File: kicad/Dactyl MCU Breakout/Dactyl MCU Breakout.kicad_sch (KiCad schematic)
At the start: 0 parts

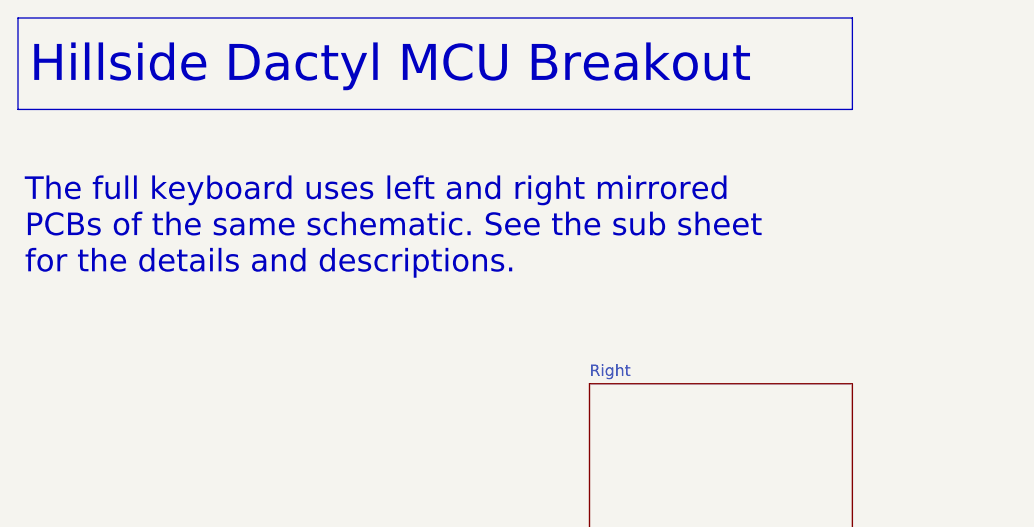
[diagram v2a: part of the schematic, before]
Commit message: feat: area reserved for TRRS. base plate notch
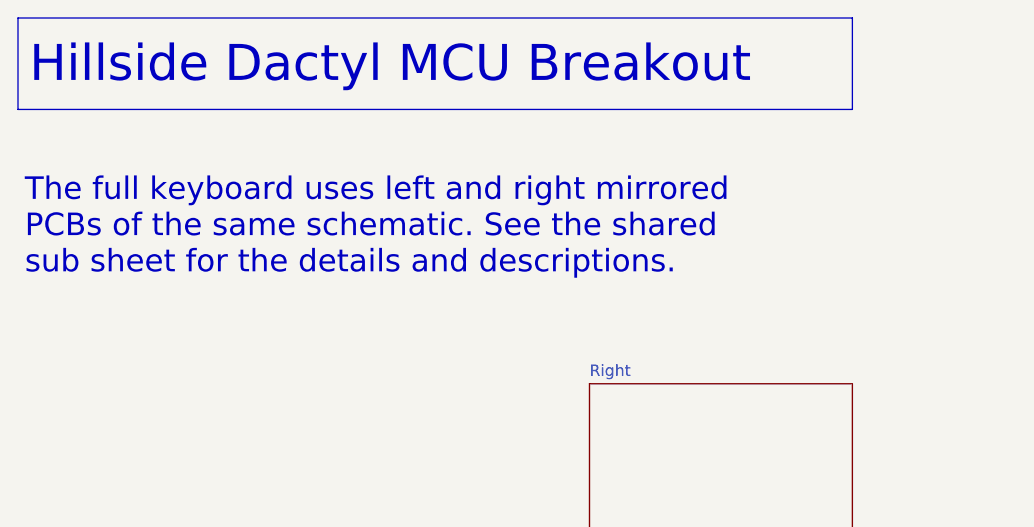
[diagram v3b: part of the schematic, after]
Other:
- note added: "The full keyboard uses left and right mirrored PCBs of the same schematic. See the shared sub sheet for the details and descriptions."
- note removed: "The full keyboard uses left and right mirrored PCBs of the same schematic. See the sub sheet for the details and descriptions."
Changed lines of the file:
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@@
 		)
 	)
-	(text "The full keyboard uses left and right mirrored  \nPCBs of the same schematic. See the sub sheet \nfor the details and descriptions."
+	(text "The full keyboard uses left and right mirrored  \nPCBs of the same schematic. See the shared \nsub sheet for the details and descriptions."
 		(exclude_from_sim no)
 		(at 94.742 99.822 0)

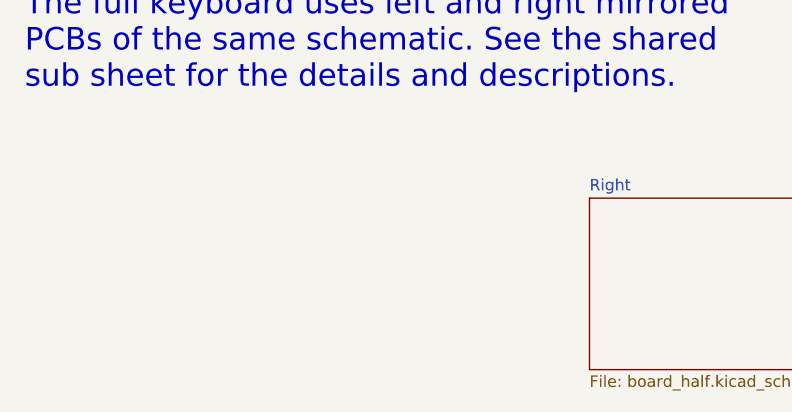
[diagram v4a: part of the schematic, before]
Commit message: feat(pcb): left half re-numbered and some routed
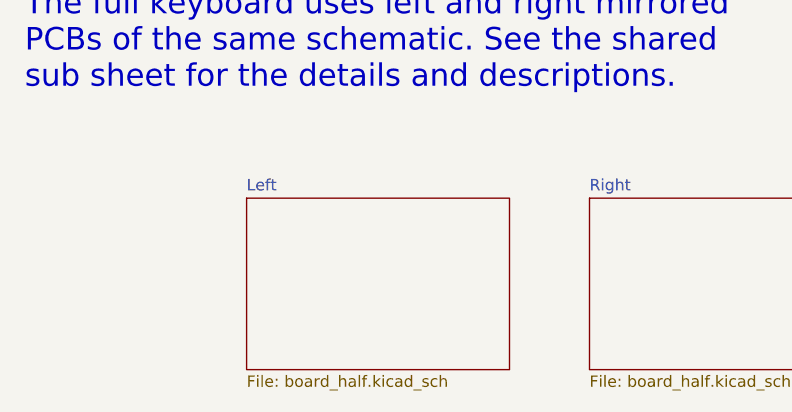
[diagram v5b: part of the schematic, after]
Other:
- added sheet Left (board_half.kicad_sch)
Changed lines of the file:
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@@
+	)
+	(sheet
+		(at 119.38 111.76)
+		(size 29.21 19.05)
+		(fields_autoplaced yes)
+		(stroke
+			(width 0.1524)
+			(type solid)
+		)
+		(fill
+			(color 255 229 191 1.0000)
+		)
+		(property "Sheetname" "Left"
+			(at 119.38 111.0484 0)
+			(effects
+				(font
+					(size 1.27 1.27)
+				)
+				(justify left bottom)
+			)
+		)
+		(property "Sheetfile" "board_half.kicad_sch"
+			(at 119.38 131.3946 0)
+			(effects
+				(font
+					(size 1.27 1.27)
+				)
+				(justify left top)
+			)
+		)
+		(instances
+			(project "Dactyl MCU Breakout"
+				(path "/454146f1-d25e-490f-a0db-4f993607d919"
+					(page "3")
+				)
+			)
+		)
 	)
 	(sheet

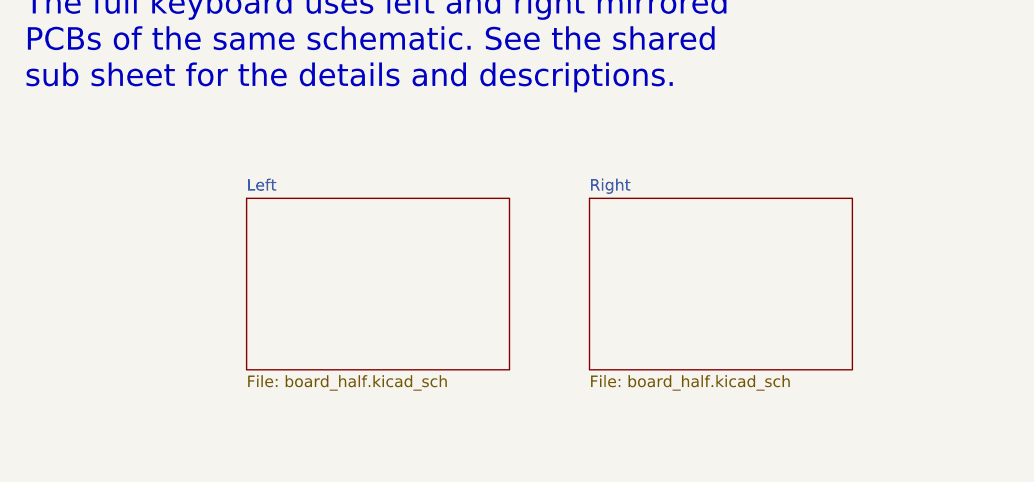
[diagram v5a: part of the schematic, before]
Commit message: feat: handedness jumper only on left board
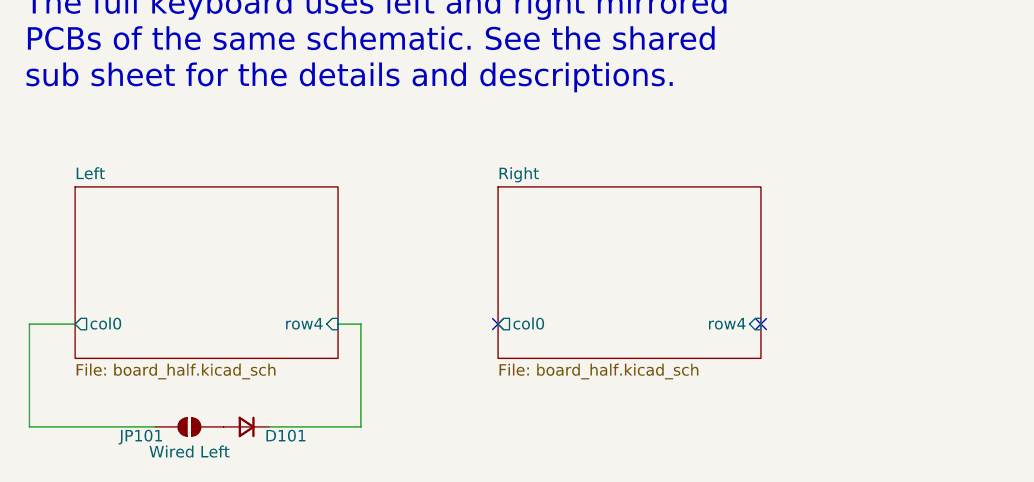
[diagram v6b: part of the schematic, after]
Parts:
- added D101: D_Small, Diode_SMD:D_SOD-323, symbol Device:D_Small
- added JP101: Wired Left, Dactyl_basics:SolderJumper-2_P1.3mm_Open_RoundedPad1.0x1.5mm, symbol Jumper:SolderJumper_2_Open
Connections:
- new net: D101.2 (A), JP101.2 (B)
- new net Left/col0: JP101.1 (A)
- new net Left/row4: D101.1 (K)
- no-connect marks 0 -> 2
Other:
- sheet Left ports: added col0, row4; removed none
- sheet Right ports: added col0, row4; removed none

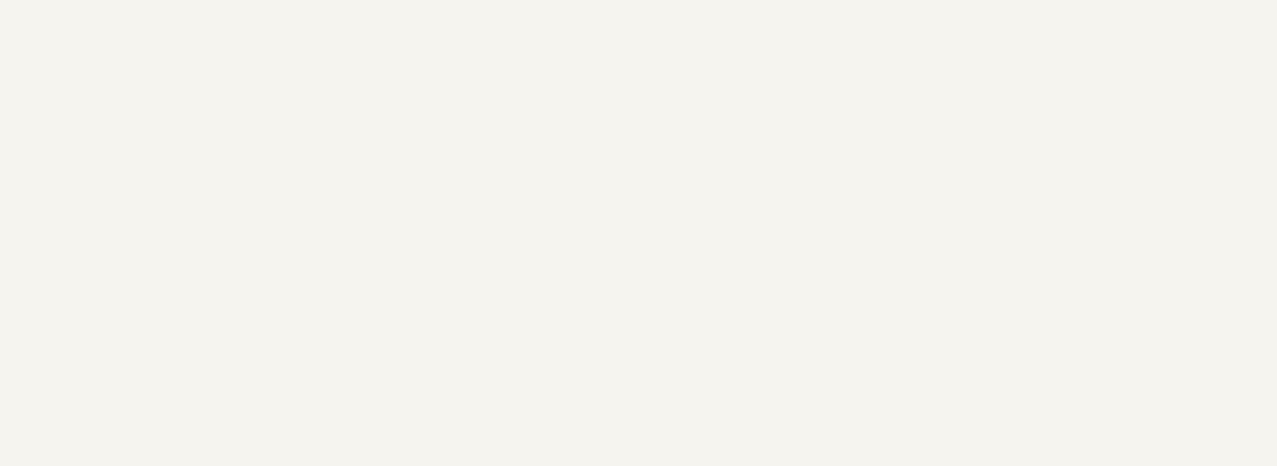
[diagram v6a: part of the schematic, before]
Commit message: feat: larger close capacitors, top/bottom fill
- Solder jumpers for split or battery to reduce the risk of attaching both.
- Wider 0.5 mm tracks for power.
- LED isolation capacitors have smaller loop distance and higher uF within size.
- USB shield ground routed to mount hole pad, as no better place to go.
- Ground fill for top and bottom layers, as well as the middle layer ones.
- Artwork in copper of a small house on a wooded hillside next to a stream.
- Rail copper fills without isolated fill warnings.
- Test point for split data line.
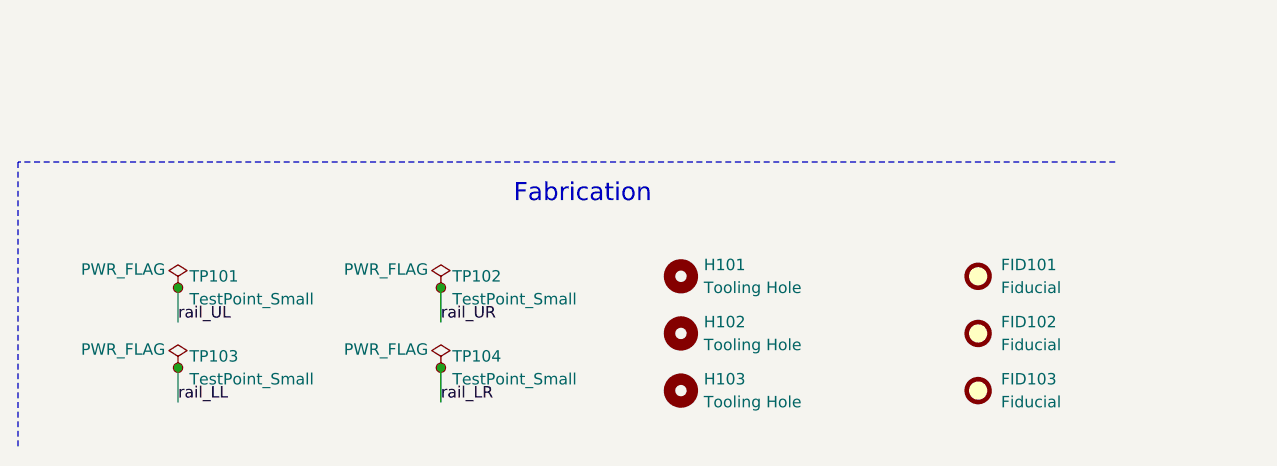
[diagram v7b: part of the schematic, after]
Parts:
- added FID101, FID102, FID103: Fiducial, Dactyl_basics:Fiducial_1mm_Mask2mm, symbol Mechanical:Fiducial
- added H101, H102, H103: Tooling Hole, Dactyl_basics:ToolingHole_1.152mm, symbol Mechanical:MountingHole
- added TP101, TP102, TP103, TP104: TestPoint_Small, TestPoint:TestPoint_THTPad_D1.0mm_Drill0.5mm, symbol Connector:TestPoint_Small
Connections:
- new net rail_LL: TP103.1
- new net rail_LR: TP104.1
- new net rail_UL: TP101.1
- new net rail_UR: TP102.1
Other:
- note added: "Fabrication"

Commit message: feat: cleanup art layout
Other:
- note added: "KiCad"
- note added: "The keyboard uses left and right mirrored PCBs of the same schematic. See the shared sub sheet for details and descriptions."
- note removed: "The full keyboard uses left and right mirrored PCBs of the same schematic. See the shared sub sheet for the details and descriptions."
- moved on the sheet: FID101, FID102, FID103, H101, H102, H103, TP101, TP102, TP103, TP104
